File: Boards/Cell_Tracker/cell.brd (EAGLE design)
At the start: 40.6 x 41.9 mm, 26 parts, among them U2 LMR16020

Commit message: General board parts placement for BITS
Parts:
- moved U$2 37.1 mm to (20.3, 24.1)
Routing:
- net +3V3: track 133.2 -> 140.6 mm
- net N$11: track 1.40 -> 5.70 mm
- net N$5: track 0.05 -> 4.10 mm
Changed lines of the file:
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@@
 <?xml version="1.0" encoding="utf-8"?>
 <!DOCTYPE eagle SYSTEM "eagle.dtd">
-<eagle version="9.3.0">
+<eagle version="7.6.0">
 <drawing>
 <settings>
 <setting alwaysvectorfont="no"/>
-<setting keepoldvectorfont="yes"/>
 <setting verticaltext="up"/>
 </settings>
@@
 <param name="dpMaxLengthDifference" value="10mm"/>
 <param name="dpGapFactor" value="2.5"/>
+<param name="checkGrid" value="0"/>
 <param name="checkAngle" value="0"/>
 <param name="checkFont" value="1"/>
 <param name="checkRestrict" value="1"/>
-<param name="checkStop" value="0"/>
-<param name="checkValues" value="0"/>
-<param name="checkNames" value="1"/>
-<param name="checkWireStubs" value="1"/>
-<param name="checkPolygonWidth" value="0"/>
 <param name="useDiameter" value="13"/>
 <param name="maxErrors" value="50"/>
@@
 </element>
 <element name="U$3" library="NR_connectors" package="MICRO_SD_HINGED" value="MICRO_SD" x="31.035625" y="15.5575" smashed="yes"/>
-<element name="U$2" library="cmdLibs" package="SC-75" value="SI1013" x="-2.54" y="-5.08" smashed="yes">
-<attribute name="NAME" x="-0.762" y="-4.191" size="0.3048" layer="25"/>
-<attribute name="VALUE" x="-0.762" y="-4.572" size="0.254" layer="27"/>
+<element name="U$2" library="cmdLibs" package="SC-75" value="SI1013" x="20.32" y="24.13" smashed="yes">
+<attribute name="NAME" x="22.098" y="25.019" size="0.3048" layer="25"/>
+<attribute name="VALUE" x="22.098" y="24.638" size="0.254" layer="27"/>
 </element>
 </elements>
@@
 <wire x1="13.255625" y1="19.129375" x2="13.255625" y2="20.716875" width="0.4064" layer="1"/>
 <wire x1="13.255625" y1="20.716875" x2="14.684375" y2="22.145625" width="0.4064" layer="1"/>
-<wire x1="14.684375" y1="22.145625" x2="15.534375" y2="22.145625" width="0.4064" layer="1"/>
 <wire x1="29.749625" y1="35.30625" x2="27.86025" y2="33.416875" width="0.4064" layer="16"/>
 <wire x1="27.86025" y1="33.416875" x2="4.92125" y2="33.416875" width="0.4064" layer="16"/>
@@
 <wire x1="24.60625" y1="4.60375" x2="25.55875" y2="5.55625" width="0.4064" layer="16"/>
 <contactref element="U$2" pad="P$2"/>
-<wire x1="16.557625" y1="3.278875" x2="18.76425" y2="3.278875" width="0" layer="19" extent="1-1"/>
-<wire x1="15.875" y1="4.9525" x2="16.557625" y2="3.278875" width="0" layer="19" extent="1-1"/>
-<wire x1="14.366875" y1="3.278875" x2="16.557625" y2="3.278875" width="0" layer="19" extent="1-1"/>
-<wire x1="-1.36" y1="-4.829" x2="14.366875" y2="3.278875" width="0" layer="19" extent="1-1"/>
+<wire x1="14.684375" y1="22.145625" x2="20.0025" y2="22.145625" width="0.4064" layer="1"/>
+<wire x1="20.0025" y1="22.145625" x2="21.510625" y2="23.65375" width="0.4064" layer="1"/>
+<wire x1="21.510625" y1="23.65375" x2="21.510625" y2="24.370375" width="0.4064" layer="1"/>
+<wire x1="21.510625" y1="24.370375" x2="21.5" y2="24.381" width="0.4064" layer="1"/>
 </signal>
 <signal name="RX3">
@@
 <wire x1="24.82785" y1="25.26665" x2="25.04175" y2="25.05275" width="0.4064" layer="1"/>
 <contactref element="U$2" pad="P$3"/>
-<wire x1="-1.854" y1="-3.53" x2="25.04175" y2="23.95275" width="0" layer="19" extent="1-1"/>
+<wire x1="21.006" y1="25.68" x2="21.63325" y2="25.05275" width="0.4064" layer="1"/>
+<wire x1="21.63325" y1="25.05275" x2="25.04175" y2="25.05275" width="0.4064" layer="1"/>
 </signal>
 <signal name="V_BCKP">
@@
 <wire x1="17.23935" y1="26.23185" x2="17.20125" y2="26.19375" width="0.4064" layer="1"/>
 <contactref element="U$2" pad="P$1"/>
-<wire x1="-2.362" y1="-4.829" x2="17.20125" y2="26.19375" width="0" layer="19" extent="1-1"/>
+<wire x1="20.498" y1="24.381" x2="19.014" y2="24.381" width="0.4064" layer="1"/>
+<wire x1="19.014" y1="24.381" x2="17.20125" y2="26.19375" width="0.4064" layer="1"/>
 </signal>
 <signal name="N$10">
@@
 </signal>
 </signals>
-<mfgpreviewcolors>
-<mfgpreviewcolor name="soldermaskcolor" color="0xC8008000"/>
-<mfgpreviewcolor name="silkscreencolor" color="0xFFFEFEFE"/>
-<mfgpreviewcolor name="backgroundcolor" color="0xFF282828"/>
-<mfgpreviewcolor name="coppercolor" color="0xFFFFBF00"/>
-<mfgpreviewcolor name="substratecolor" color="0xFF786E46"/>
-</mfgpreviewcolors>
 <errors>
 </errors>

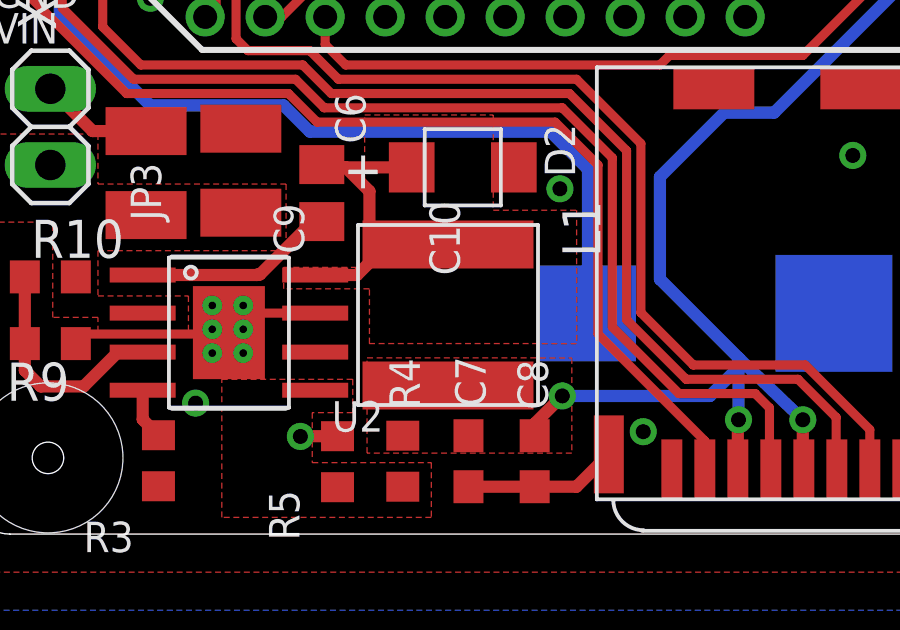
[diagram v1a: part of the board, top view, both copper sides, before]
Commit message: Updated the inductor and mosfet in cell schematic
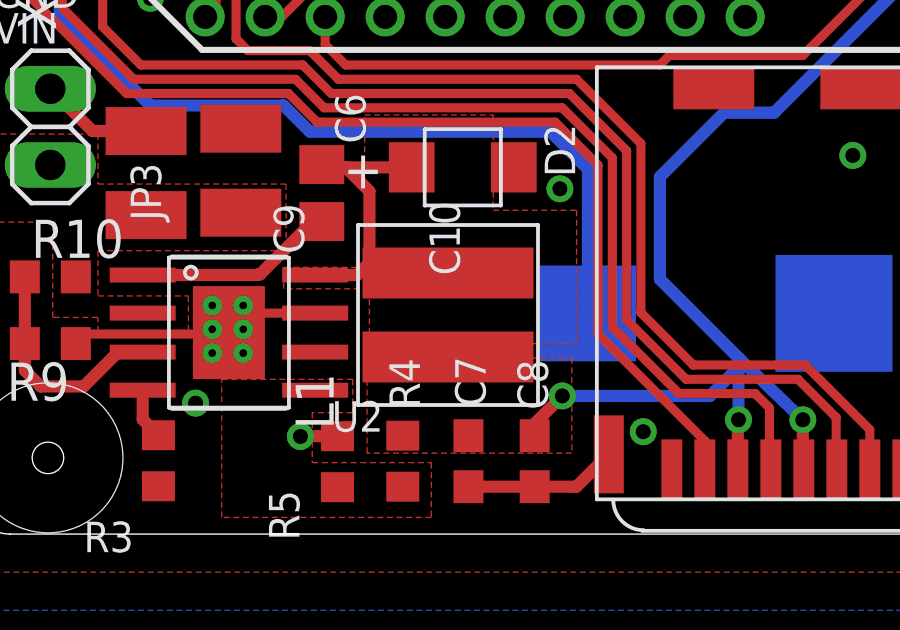
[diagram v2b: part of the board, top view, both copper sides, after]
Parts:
- L1: value (none) -> ASPI-6045S-560M-TCT-ND; device inductors:TAIYO_YUDEN_NONSTANDARD -> inductors:ABRACON
- R10: value 196k -> 190k
- turned L1 to 90 degrees
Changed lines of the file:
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@@
 <attribute name="VALUE" x="3.254375" y="8.255" size="1.27" layer="27" rot="R180"/>
 </element>
-<element name="R10" library="resistor" package="R0603" value="196k" x="2.619375" y="8.5725" smashed="yes">
+<element name="R10" library="resistor" package="R0603" value="190k" x="2.619375" y="8.5725" smashed="yes">
 <attribute name="NAME" x="1.984375" y="9.2075" size="1.27" layer="25"/>
 <attribute name="VALUE" x="1.984375" y="6.6675" size="1.27" layer="27"/>
 </element>
-<element name="L1" library="inductors" package="TAIYO_YUDEN_NONSTANDARD" value="" x="15.875" y="7.3025" smashed="yes" rot="R270">
-<attribute name="NAME" x="19.685" y="11.1125" size="1.27" layer="25" rot="R270"/>
-<attribute name="VALUE" x="10.795" y="11.1125" size="1.27" layer="27" rot="R270"/>
+<element name="L1" library="inductors" package="ABRACON" value="ASPI-6045S-560M-TCT-ND" x="15.875" y="7.3025" smashed="yes" rot="R90">
+<attribute name="NAME" x="12.065" y="3.4925" size="1.27" layer="25" rot="R90"/>
+<attribute name="VALUE" x="20.955" y="3.4925" size="1.27" layer="27" rot="R90"/>
 </element>
 <element name="U$3" library="NR_connectors" package="MICRO_SD_HINGED" value="MICRO_SD" x="31.035625" y="15.5575" smashed="yes"/>

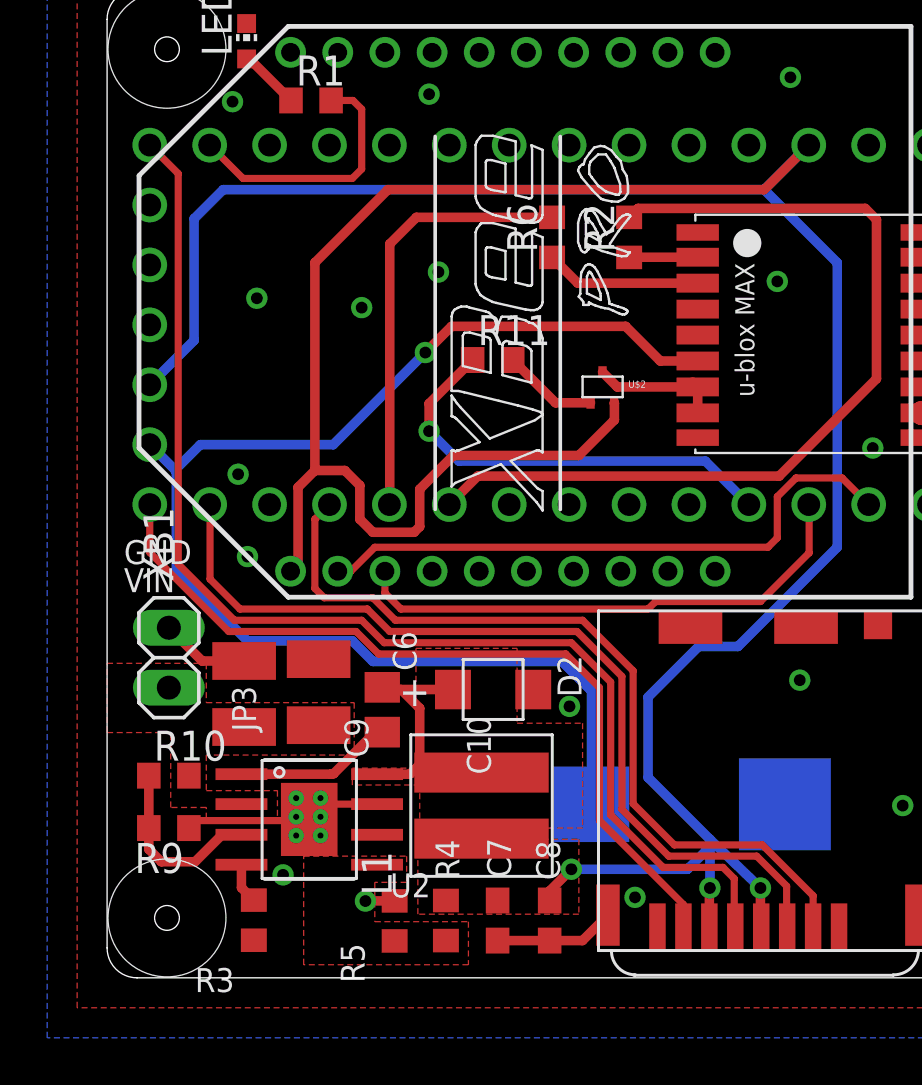
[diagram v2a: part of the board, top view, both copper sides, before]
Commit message: put connector on cell board, plus lots of cad work
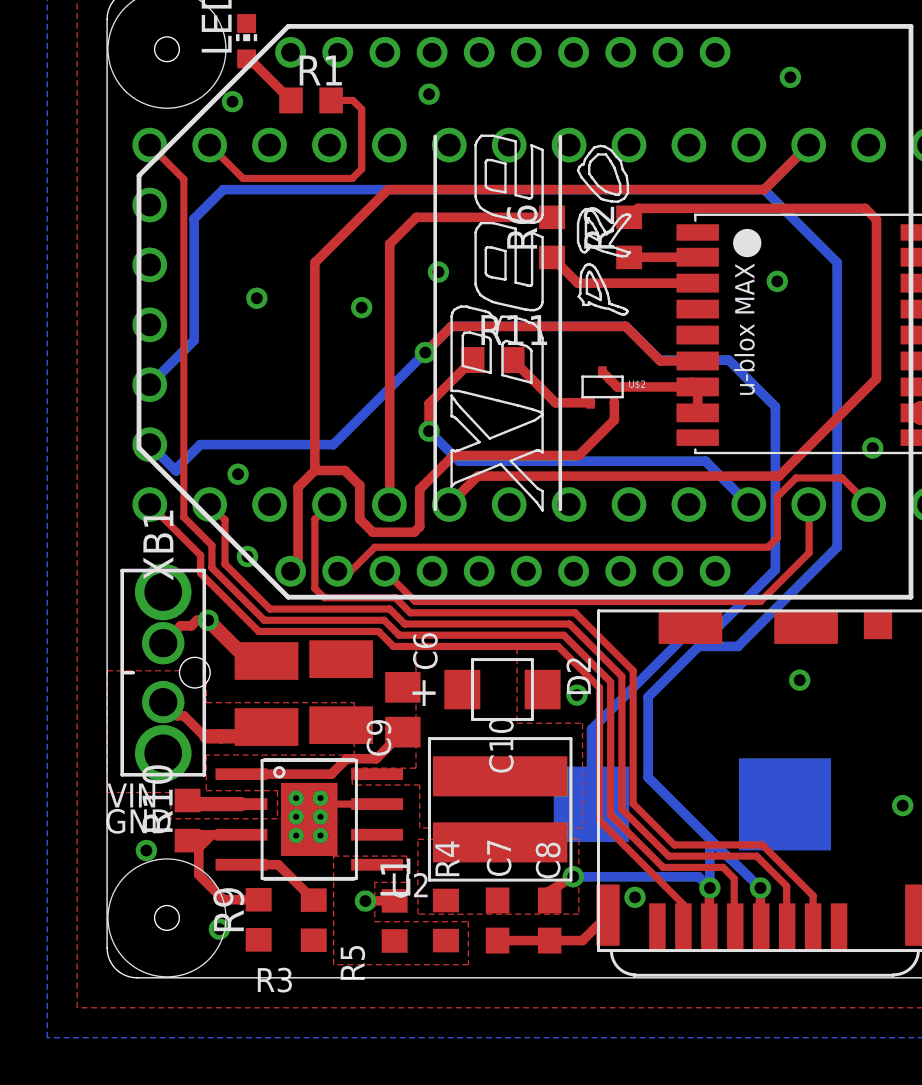
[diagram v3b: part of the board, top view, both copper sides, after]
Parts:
- removed JP3: (no value), pinhead:1X02
- added U$4: MOLEX_NANOFIT_2, cmdLibs:MOLEX_NANOFIT_2
- moved R9 5.44 mm to (6.43, 2.46), turned to 90 degrees
- moved R3 2.54 mm to (8.76, 2.44)
- moved R10 2.06 mm to (3.41, 6.67), turned to 90 degrees
- moved C10 0.95 mm to (9.92, 12.1)
- moved C9 0.95 mm to (6.76, 12.0)
- moved C6 0.87 mm to (12.5, 11.4)
- moved L1 0.81 mm to (16.7, 7.14)
- moved D2 0.40 mm to (16.8, 12.2)
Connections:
- net GND: now also U$4.P$1; no longer JP3.1
- net VIN: now also U$4.P$2; no longer JP3.2
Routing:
- net V_BCKP: track 55.6 -> 64.3 mm
- net SW: track 8.52 -> 0.00 mm
- net VIN: track 0.00 -> 8.13 mm
- net GND: track 17.4 -> 14.4 mm, vias 22 -> 24
- net N$8: track 1.72 -> 3.69 mm
- net TX1: track 22.2 -> 21.4 mm
- net SCK: track 52.7 -> 52.0 mm
- net MOSI: track 38.0 -> 37.3 mm
- net MISO: track 35.1 -> 34.3 mm

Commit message: All of the changes with CAD and electronics since switching to the microclasp connectors
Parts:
- added R7: (no value), resistor:R0603
- added U$5: (no value), NR_connectors:MICROCLASP
- U$4: value MOLEX_NANOFIT_2 -> (none); device cmdLibs:MOLEX_NANOFIT_2 -> NR_connectors:MICROCLASP
- moved U$4 37.6 mm to (39.8, 9.05), turned to 270 degrees
- moved R10 31.8 mm to (35.2, 7.70), turned to 270 degrees
- moved R9 29.9 mm to (35.2, 10.8), turned to 270 degrees
- moved C9 29.2 mm to (34.6, 3.29), turned to 270 degrees
- moved R3 28.8 mm to (35.1, 13.9), turned to 270 degrees
- moved C10 23.3 mm to (31.4, 3.29), turned to 270 degrees
- moved U2 21.6 mm to (30.0, 9.56), turned to 90 degrees
- moved R5 21.0 mm to (30.0, 13.4), turned to 180 degrees
- moved C6 17.8 mm to (28.7, 3.71), turned to 90 degrees
- moved COIN 16.7 mm to (12.1, 7.20)
- moved R4 16.5 mm to (26.7, 13.4), turned to 180 degrees
- moved U$3 15.5 mm to (15.6, 15.5)
- moved C8 12.6 mm to (23.9, 14.0), turned to 90 degrees
- moved C7 12.6 mm to (21.5, 14.0), turned to 90 degrees
- moved D2 11.0 mm to (24.6, 4.52), turned to 0 degrees
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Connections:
- new net N$12: R7.1, U$5.P$1
- new net N$15: U$1.4
- new net N$16: U$1.5
- new net N$33: U$1.6
- new net SWITCH_LED: R7.2, U$1.3
- net GND: now also U$4.P$2, U$5.P$2; no longer U$4.P$1
- net VIN: now also U$4.P$1; no longer U$4.P$2
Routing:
- net +3V3: track 140.1 -> 100.3 mm, vias 3 -> 2
- net V_BCKP: track 64.3 -> 41.8 mm, vias 1 -> 3
- net SWITCH_LED: track 0.00 -> 13.8 mm
- net MISO: track 34.3 -> 20.9 mm
- net SCK: track 52.0 -> 38.9 mm
- net MOSI: track 37.3 -> 24.7 mm
- net GND: track 14.4 -> 2.50 mm, vias 24 -> 22
- net SD_CS: track 35.0 -> 28.8 mm
- net N$12: track 0.00 -> 5.04 mm
- net VIN: track 8.13 -> 3.49 mm
- net FB: track 0.00 -> 3.76 mm
- net EN: track 7.29 -> 3.79 mm
- net N$9: track 7.58 -> 5.84 mm
- net N$8: track 3.69 -> 2.91 mm
- removed copper zone on layer 1, net FB
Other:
- board size 40.6 x 41.9 mm -> 43.2 x 41.9 mm
